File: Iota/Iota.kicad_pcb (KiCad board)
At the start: 2 copper layers, 31.8 x 54.6 mm, 25 parts, among them J1 USB_B_Mini, J2 Conn_01x12_Male, J3 Conn_01x12_Male, J4 ICSP, U1 ATmega32U4-AU, Y1 16MHz

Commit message: Working on PCB layout
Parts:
- moved J1 3.24 mm to (133.3, 61.8)
- moved C6 2.73 mm to (133.2, 66.1)
- moved R7 2.64 mm to (138.9, 66.8)
- moved R5 2.59 mm to (136.9, 66.8)
- moved D2 1.83 mm to (127.0, 62.1), turned to 270 degrees
- moved F1 1.52 mm to (133.4, 68.4)
- moved R11 1.40 mm to (127.0, 66.2), turned to 270 degrees
- moved C13 0.58 mm to (133.4, 70.9)
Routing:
- net UVCC: track 19.2 -> 0.09 mm
- net D+: track 17.3 -> 0.00 mm, vias 2 -> 0
- net VCC: track 14.2 -> 0.00 mm, vias 2 -> 0
- net Net-(D2-Pad2): track 3.77 -> 0.00 mm
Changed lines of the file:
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@@
     (thickness 1.6)
     (drawings 4)
-    (tracks 35)
+    (tracks 2)
     (zones 0)
     (modules 25)
@@
   )
   (module Resistors_SMD:R_0805 (layer F.Cu)
-    (at 140.0175 64.3865 90)
+    (at 138.938 66.7995 90)
     (descr "Resistor SMD 0805, reflow soldering, Vishay (see dcrcw.pdf)")
     (tags "resistor 0805")
@@
   )
   (module Connectors:USB_Micro-B (layer F.Cu)
-    (at 133.4135 58.6105 180)
+    (at 133.2865 61.849 180)
     (descr "Micro USB Type B Receptacle")
     (tags "USB USB_B USB_micro USB_OTG")
@@
   )
   (module Capacitors_SMD:C_0805 (layer F.Cu)
-    (at 133.366 70.2945)
+    (at 133.4295 70.866)
     (descr "Capacitor SMD 0805, reflow soldering, AVX (see smccp.pdf)")
     (tags "capacitor 0805")
@@
   )
   (module Resistors_SMD:R_0805 (layer F.Cu)
-    (at 137.8585 64.3865 90)
+    (at 136.906 66.7995 90)
     (descr "Resistor SMD 0805, reflow soldering, Vishay (see dcrcw.pdf)")
     (tags "resistor 0805")
@@
   )
   (module Resistors_SMD:R_0805 (layer F.Cu)
-    (at 127.8915 67.2465)
+    (at 127 66.167 270)
     (descr "Resistor SMD 0805, reflow soldering, Vishay (see dcrcw.pdf)")
     (tags "resistor 0805")
     (attr smd)
-    (fp_text reference R11 (at 0.061 0.0635) (layer F.SilkS)
-      (effects (font (size 1 1) (thickness 0.15)))
-    )
-    (fp_text value 1K (at -0.0025 0.127) (layer F.Fab)
-      (effects (font (size 1 1) (thickness 0.15)))
-    )
-    (fp_text user %R (at 0 0) (layer F.Fab)
+    (fp_text reference R11 (at 0.061 0.0635 270) (layer F.SilkS)
+      (effects (font (size 1 1) (thickness 0.15)))
+    )
+    (fp_text value 1K (at -0.0025 0.127 270) (layer F.Fab)
+      (effects (font (size 1 1) (thickness 0.15)))
+    )
+    (fp_text user %R (at 0 0 270) (layer F.Fab)
       (effects (font (size 0.5 0.5) (thickness 0.075)))
     )
@@
     (fp_line (start 1.55 0.9) (end 1.55 -0.9) (layer F.CrtYd) (width 0.05))
     (fp_line (start 1.55 0.9) (end -1.55 0.9) (layer F.CrtYd) (width 0.05))
-    (pad 1 smd rect (at -0.95 0) (size 0.7 1.3) (layers F.Cu F.Paste F.Mask)
+    (pad 1 smd rect (at -0.95 0 270) (size 0.7 1.3) (layers F.Cu F.Paste F.Mask)
       (net 41 "Net-(D2-Pad2)"))
-    (pad 2 smd rect (at 0.95 0) (size 0.7 1.3) (layers F.Cu F.Paste F.Mask)
+    (pad 2 smd rect (at 0.95 0 270) (size 0.7 1.3) (layers F.Cu F.Paste F.Mask)
       (net 6 VCC))
     (model ${KISYS3DMOD}/Resistors_SMD.3dshapes/R_0805.wrl
@@
   )
   (module Capacitors_SMD:C_0805 (layer F.Cu)
-    (at 133.3025 63.373)
+    (at 133.239 66.1035)
     (descr "Capacitor SMD 0805, reflow soldering, AVX (see smccp.pdf)")
     (tags "capacitor 0805")
     (attr smd)
-    (fp_text reference C6 (at 0 -1.5) (layer F.SilkS)
+    (fp_text reference C6 (at 0 0) (layer F.SilkS)
       (effects (font (size 1 1) (thickness 0.15)))
     )
@@
   )
   (module Diodes_SMD:D_1206 (layer F.Cu)
-    (at 127.86686 63.713672 180)
+    (at 127 62.103 270)
     (descr "Diode SMD 1206, reflow soldering http://datasheets.avx.com/schottky.pdf")
     (tags "Diode 1206")
     (attr smd)
-    (fp_text reference D2 (at -0.02214 0.023172 180) (layer F.SilkS)
-      (effects (font (size 1 1) (thickness 0.15)))
-    )
-    (fp_text value red (at -0.02214 0.150172 180) (layer F.Fab)
+    (fp_text reference D2 (at -0.02214 0.023172 270) (layer F.SilkS)
+      (effects (font (size 1 1) (thickness 0.15)))
+    )
+    (fp_text value red (at -0.02214 0.150172 270) (layer F.Fab)
       (effects (font (size 1 1) (thickness 0.15)))
     )
@@
     (fp_line (start 0.127 0) (end 0.381 0) (layer F.Fab) (width 0.1))
     (fp_line (start -0.254 -0.254) (end -0.254 0.254) (layer F.Fab) (width 0.1))
-    (fp_text user %R (at -0.02214 0.023172 180) (layer F.Fab)
-      (effects (font (size 1 1) (thickness 0.15)))
-    )
-    (pad 2 smd rect (at 1.5 0 180) (size 1 1.6) (layers F.Cu F.Paste F.Mask)
+    (fp_text user %R (at -0.02214 0.023172 270) (layer F.Fab)
+      (effects (font (size 1 1) (thickness 0.15)))
+    )
+    (pad 2 smd rect (at 1.5 0 270) (size 1 1.6) (layers F.Cu F.Paste F.Mask)
       (net 41 "Net-(D2-Pad2)"))
-    (pad 1 smd rect (at -1.5 0 180) (size 1 1.6) (layers F.Cu F.Paste F.Mask)
+    (pad 1 smd rect (at -1.5 0 270) (size 1 1.6) (layers F.Cu F.Paste F.Mask)
       (net 1 GND))
     (model ${KISYS3DMOD}/Diodes_SMD.3dshapes/D_1206.wrl
@@
   )
   (module Resistors_SMD:R_1206 (layer F.Cu)
-    (at 133.35 66.8655)
+    (at 133.3605 68.3895)
     (descr "Resistor SMD 1206, reflow soldering, Vishay (see dcrcw.pdf)")
     (tags "resistor 1206")
     (attr smd)
-    (fp_text reference F1 (at 0.0635 -3.429) (layer F.SilkS)
+    (fp_text reference F1 (at 0.0635 0) (layer F.SilkS)
       (effects (font (size 1 1) (thickness 0.15)))
     )
@@
   (gr_line (start 149.225 55.1815) (end 149.225 109.7915) (layer Edge.Cuts) (width 0.15))
   (gr_line (start 117.5385 55.1815) (end 149.225 55.1815) (layer Edge.Cuts) (width 0.15))
-  (segment (start 132.1135 59.9605) (end 130.9135 59.9605) (width 0.25) (layer F.Cu) (net 1))
-  (segment (start 134.3025 66.368) (end 134.8 66.8655) (width 0.25) (layer F.Cu) (net 4))
-  (segment (start 134.3025 63.373) (end 134.3025 66.368) (width 0.25) (layer F.Cu) (net 4))
-  (segment (start 134.366 63.3095) (end 134.3025 63.373) (width 0.25) (layer F.Cu) (net 4))
-  (segment (start 134.7135 62.962) (end 134.3025 63.373) (width 0.25) (layer F.Cu) (net 4))
-  (segment (start 134.7135 59.9605) (end 134.7135 62.962) (width 0.25) (layer F.Cu) (net 4))
-  (segment (start 132.541483 76.327) (end 132.437273 76.22279) (width 0.25) (layer F.Cu) (net 4))
-  (segment (start 132.651276 76.327) (end 132.541483 76.327) (width 0.25) (layer F.Cu) (net 4))
-  (segment (start 135.191001 68.356501) (end 135.191001 73.787275) (width 0.25) (layer F.Cu) (net 4))
-  (segment (start 132.437273 76.22279) (end 131.836233 75.62175) (width 0.25) (layer F.Cu) (net 4))
-  (segment (start 135.191001 73.787275) (end 132.651276 76.327) (width 0.25) (layer F.Cu) (net 4))
-  (segment (start 134.8 67.9655) (end 135.191001 68.356501) (width 0.25) (layer F.Cu) (net 4))
-  (segment (start 134.8 66.8655) (end 134.8 67.9655) (width 0.25) (layer F.Cu) (net 4))
-  (segment (start 131.519 67.2465) (end 131.9 66.8655) (width 0.25) (layer F.Cu) (net 6))
-  (segment (start 128.8415 67.2465) (end 131.519 67.2465) (width 0.25) (layer F.Cu) (net 6))
-  (segment (start 131.9 69.8285) (end 132.366 70.2945) (width 0.25) (layer F.Cu) (net 6))
-  (segment (start 131.9 66.8655) (end 131.9 69.8285) (width 0.25) (layer F.Cu) (net 6))
-  (via (at 133.096 71.882) (size 0.8) (drill 0.4) (layers F.Cu B.Cu) (net 6))
-  (segment (start 132.366 71.152) (end 133.096 71.882) (width 0.25) (layer F.Cu) (net 6))
-  (segment (start 132.366 70.2945) (end 132.366 71.152) (width 0.25) (layer F.Cu) (net 6))
-  (via (at 135.916001 73.533) (size 0.8) (drill 0.4) (layers F.Cu B.Cu) (net 6))
-  (segment (start 134.747 73.533) (end 135.916001 73.533) (width 0.25) (layer B.Cu) (net 6))
-  (segment (start 133.096 71.882) (end 134.747 73.533) (width 0.25) (layer B.Cu) (net 6))
-  (segment (start 135.916001 73.946145) (end 134.806082 75.056064) (width 0.25) (layer F.Cu) (net 6))
-  (segment (start 135.916001 73.533) (end 135.916001 73.946145) (width 0.25) (layer F.Cu) (net 6))
-  (via (at 137.8585 66.4845) (size 0.8) (drill 0.4) (layers F.Cu B.Cu) (net 36))
-  (segment (start 137.8585 65.3365) (end 137.8585 66.4845) (width 0.25) (layer F.Cu) (net 36))
-  (via (at 129.6035 75.5015) (size 0.8) (drill 0.4) (layers F.Cu B.Cu) (net 36))
-  (segment (start 129.6035 75.651758) (end 130.704862 76.75312) (width 0.25) (layer F.Cu) (net 36))
-  (segment (start 129.6035 75.5015) (end 129.6035 75.651758) (width 0.25) (layer F.Cu) (net 36))
-  (segment (start 134.493 66.4845) (end 129.6035 71.374) (width 0.25) (layer B.Cu) (net 36))
-  (segment (start 129.6035 71.374) (end 129.6035 75.5015) (width 0.25) (layer B.Cu) (net 36))
-  (segment (start 137.8585 66.4845) (end 134.493 66.4845) (width 0.25) (layer B.Cu) (net 36))
-  (segment (start 126.36686 66.67186) (end 126.9415 67.2465) (width 0.25) (layer F.Cu) (net 41))
-  (segment (start 126.36686 63.713672) (end 126.36686 66.67186) (width 0.25) (layer F.Cu) (net 41))
+  (segment (start 132.177 63.199) (end 130.977 63.199) (width 0.25) (layer F.Cu) (net 1))
+  (segment (start 134.5565 66.04) (end 134.493 66.1035) (width 0.25) (layer F.Cu) (net 4))
   (zone (net 1) (net_name GND) (layer F.Cu) (hatch edge 0.508)
     (connect_pads (clearance 0.508))

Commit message: Still faffing around laying out tracks
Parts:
- moved D1 30.6 mm to (125.5, 65.5), turned to 90 degrees
- moved R4 21.9 mm to (125.5, 69.7), turned to 270 degrees
- moved R6 18.0 mm to (126.0, 90.2), turned to 90 degrees
- moved D3 17.2 mm to (126.0, 94.1)
- moved R11 15.2 mm to (141.8, 69.6)
- moved D2 15.2 mm to (141.8, 65.5)
- moved C3 9.79 mm to (141.0, 77.0), turned to 0 degrees
- moved F1 5.99 mm to (139.2, 69.8), turned to 90 degrees
- moved R5 5.06 mm to (132.5, 69.2)
- moved R7 5.00 mm to (134.6, 69.2)
- moved C6 4.92 mm to (136.9, 69.4), turned to 90 degrees
- moved C14 3.18 mm to (136.3, 91.2), turned to 180 degrees
- moved J2 2.80 mm to (122.2, 99.3)
- moved J1 2.79 mm to (133.3, 64.6)
- moved C1 2.70 mm to (139.6, 75.1), turned to 180 degrees
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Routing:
- net GND: track 1.20 -> 0.00 mm
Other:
- board outline removed

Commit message: Still fiddling with PCB layout
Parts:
- moved C14 0.84 mm to (137.2, 91.1)
- moved U1 0.80 mm to (134.0, 82.6), turned to 225 degrees
- moved R2 0.76 mm to (125.8, 86.7)

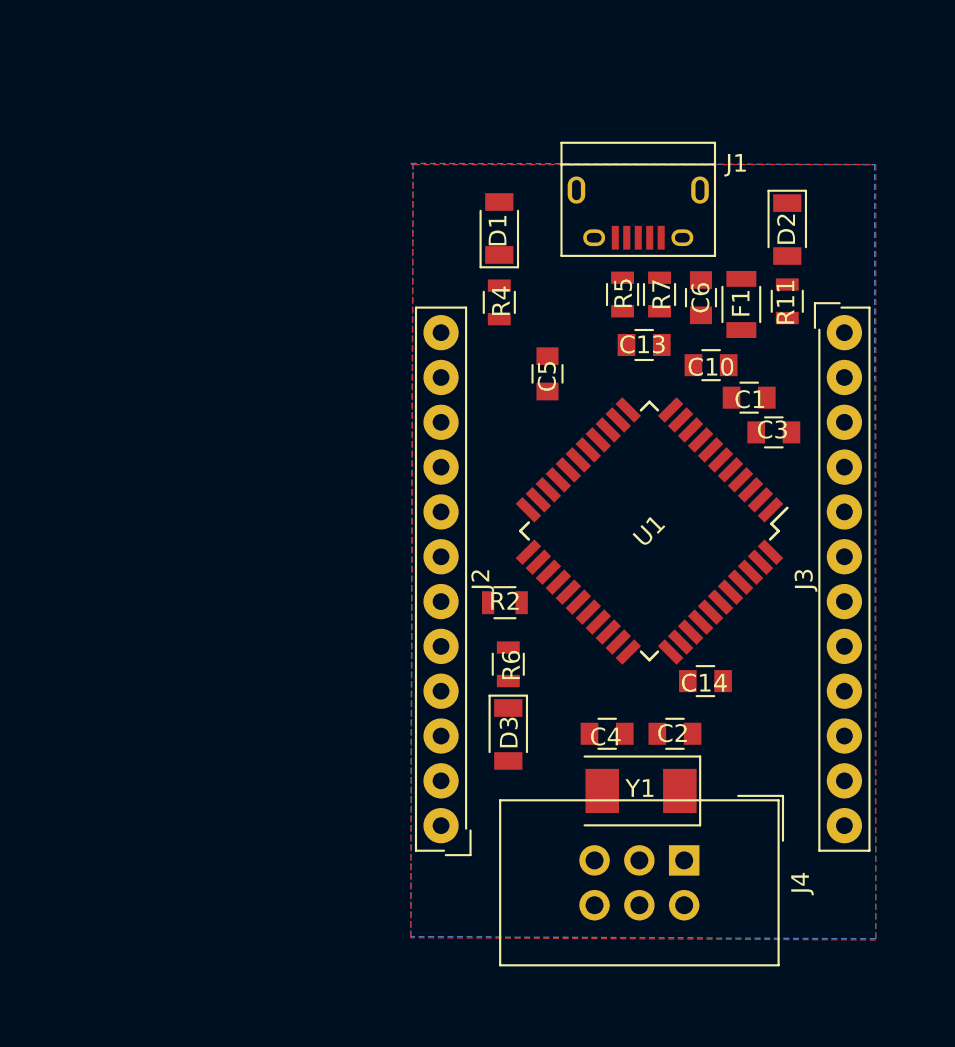
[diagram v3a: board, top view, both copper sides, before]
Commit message: Move to Teensy 2.0 clone
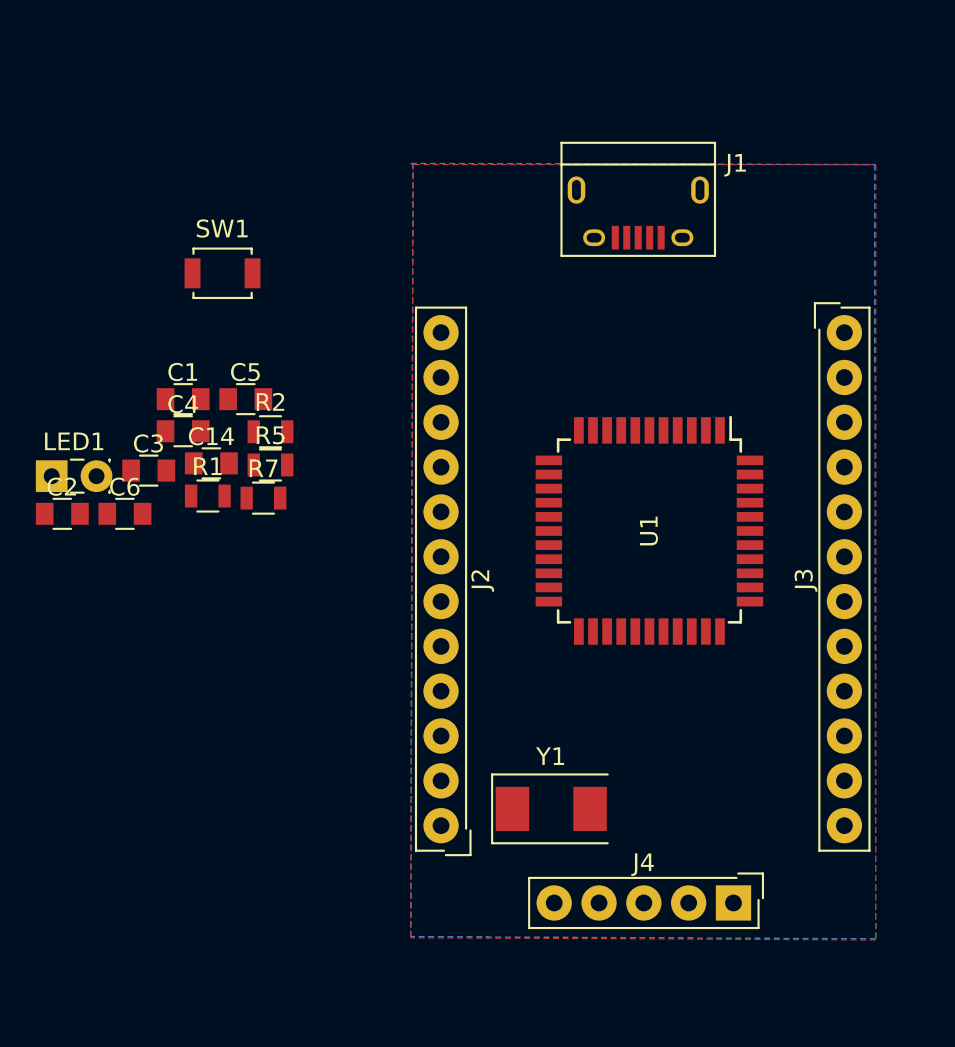
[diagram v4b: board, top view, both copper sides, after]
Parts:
- removed C10: 1uF, Capacitors_SMD:C_0805
- removed C13: 10uF, Capacitors_SMD:C_0805
- removed D1: yellow, Diodes_SMD:D_1206
- removed D2: red, Diodes_SMD:D_1206
- removed D3: green, Diodes_SMD:D_1206
- removed F1: 500mA, Resistors_SMD:R_1206
- removed R11: 1K, Resistors_SMD:R_0805
- removed R4, R6: 330, Resistors_SMD:R_0805
- added LED1: red, LEDs:LED_Rectangular_W3.9mm_H1.8mm, F.Cu at (100.1, 79.5)
- added R1: 1K0, Resistors_SMD:R_0805, F.Cu at (109.0, 80.6)
- added SW1: SW_DIP_x01, Buttons_Switches_SMD:SW_SPST_B3U-1000P, F.Cu at (109.8, 68.0)
- C2, C4: value 22pF -> 10pF
- J4: value ICSP -> Conn_01x05_Male; footprint Connectors_IDC:IDC-Header_2x03_Pitch2.54mm_Straight -> Connectors_Samtec:SL-105-X-XX_1x05
- R2: value 10K -> 1K0
- moved C2 36.9 mm to (100.7, 81.6)
- moved C3 35.5 mm to (105.6, 79.2)
- moved C6 34.9 mm to (104.3, 81.6), turned to 0 degrees
- moved C1 32.1 mm to (107.6, 75.1), turned to 0 degrees
- moved C14 30.6 mm to (109.2, 78.8), turned to 0 degrees
- moved C4 29.5 mm to (107.6, 77.0), turned to 0 degrees
- moved R7 25.2 mm to (112.1, 80.8), turned to 0 degrees
- moved R5 22.2 mm to (112.5, 78.9), turned to 0 degrees
- moved C5 17.2 mm to (111.1, 75.1), turned to 0 degrees
- moved R2 16.4 mm to (112.5, 77.0)
- moved Y1 5.19 mm to (128.4, 98.4), turned to 0 degrees
- moved J4 3.69 mm to (138.7, 103.7)
- turned U1 to 270 degrees
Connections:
- C14 pad 2: VCC -> Vcc
- C3 pad 2: VCC -> Vcc
- C6 pad 2: UVCC -> Vcc
- J1 pad 1: UVCC -> Vcc
- J2 pad 1: D9 -> C7
- J2 pad 10: GND -> B1
- J2 pad 11: RXI -> B0
- J2 pad 12: TXO -> GND
- J2 pad 2: D8 -> C6
- J2 pad 3: D7 -> D3
- J2 pad 4: D6 -> D2
- J2 pad 5: D5 -> D1
- J2 pad 6: D4 -> D0
- J2 pad 7: D3 -> B7
- J2 pad 8: D2 -> B3
- J2 pad 9: GND -> B2
- J3 pad 1: Net-(J3-Pad1) -> Vcc
- J3 pad 10: MISO -> B4
- J3 pad 11: MOSI -> D7
- J3 pad 12: D10 -> D6
- J3 pad 2: GND -> F0
- J3 pad 3: RESET -> F1
- J3 pad 4: VCC -> F4
- J3 pad 5: A3 -> F5
- J3 pad 6: A2 -> F6
- J3 pad 7: A1 -> F7
- J3 pad 8: A0 -> B6
- J3 pad 9: SCK -> B5
- J4 pad 1: MISO -> D4
- J4 pad 2: VCC -> RESET
- J4 pad 3: SCK -> GND
- J4 pad 4: MOSI -> Vcc
- J4 pad 5: RESET -> D5
- R2 pad 1: RESET -> Net-(LED1-Pad1)
- R2 pad 2: VCC -> GND
- U1 pad 1: D7 -> E6
- U1 pad 10: MOSI -> B2
- U1 pad 11: MISO -> B3
- U1 pad 12: D11 -> B7
- U1 pad 14: VCC -> Vcc
- U1 pad 18: D3 -> D0
- U1 pad 19: D2 -> D1
- U1 pad 2: UVCC -> Vcc
- U1 pad 20: RXI -> D2
- U1 pad 21: TXO -> D3
- U1 pad 22: Net-(R6-Pad2) -> D5
- U1 pad 24: VCC -> Vcc
- U1 pad 26: D12 -> D6
- U1 pad 27: D6 -> D7
- U1 pad 28: D8 -> B4
- U1 pad 29: D9 -> B5
- U1 pad 30: D10 -> B6
- U1 pad 31: D5 -> C6
- U1 pad 32: D13 -> C7
- U1 pad 33: GND -> Net-(R1-Pad2)
- U1 pad 34: VCC -> Vcc
- U1 pad 36: A0 -> F7
- U1 pad 37: A1 -> F6
- U1 pad 38: A2 -> F5
- U1 pad 39: A3 -> F4
- U1 pad 40: A4 -> F1
- U1 pad 41: A5 -> F0
- U1 pad 44: VCC -> Vcc
- U1 pad 7: UVCC -> Vcc
- U1 pad 8: Net-(R4-Pad2) -> B0
- U1 pad 9: SCK -> B1

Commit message: Switch over to Teensy 2 clone
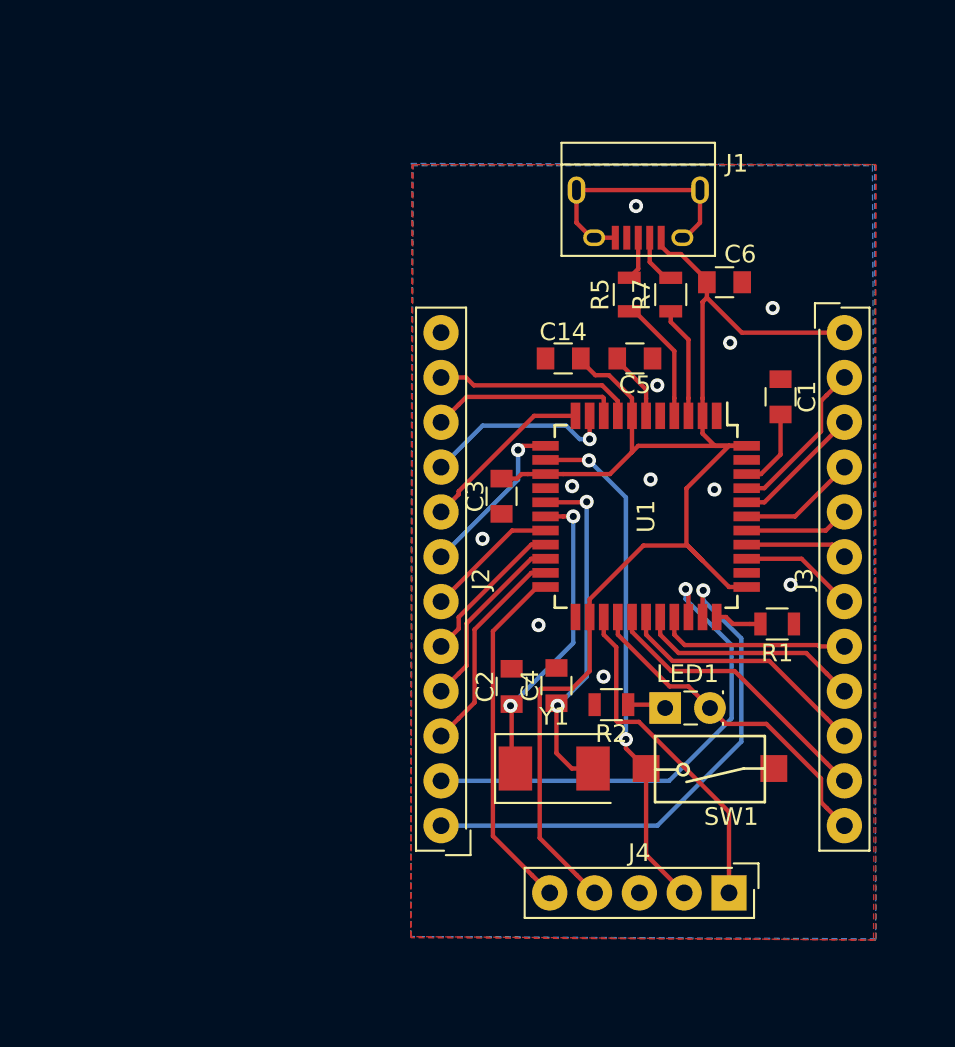
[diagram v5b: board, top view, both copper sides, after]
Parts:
- SW1: footprint Buttons_Switches_SMD:SW_SPST_B3U-1000P -> Iota:Switch
- moved SW1 39.4 mm to (137.4, 96.1), turned to 180 degrees
- moved LED1 37.2 mm to (134.9, 92.6)
- moved C6 36.4 mm to (138.2, 68.5), turned to 180 degrees
- moved C1 33.9 mm to (141.4, 75.0), turned to 270 degrees
- moved R1 33.1 mm to (141.2, 87.9), turned to 180 degrees
- moved C2 27.3 mm to (126.2, 91.4), turned to 90 degrees
- moved R7 25.8 mm to (135.2, 69.2), turned to 90 degrees
- moved C4 25.6 mm to (128.7, 91.4), turned to 90 degrees
- moved R2 24.7 mm to (131.8, 92.5), turned to 180 degrees
- moved R5 22.5 mm to (132.8, 69.2), turned to 90 degrees
- moved C5 22.2 mm to (133.2, 72.8), turned to 180 degrees
- moved C14 20.8 mm to (129.1, 72.8)
- moved C3 20.0 mm to (125.6, 80.6), turned to 90 degrees
- moved Y1 2.29 mm to (128.6, 96.1)
- moved U1 0.85 mm to (133.8, 81.8)
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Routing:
- net Vcc: track 0.00 -> 84.8 mm
- net C7: track 0.00 -> 30.0 mm, vias 0 -> 1
- net RESET: track 0.00 -> 29.6 mm, vias 0 -> 2
- net C6: track 0.00 -> 28.0 mm, vias 0 -> 1
- net D5: track 0.00 -> 20.7 mm
- net Net-(C4-Pad1): track 0.00 -> 19.8 mm, vias 0 -> 2
- net D4: track 0.00 -> 19.3 mm
- net D6: track 0.00 -> 19.1 mm
- net Net-(C2-Pad1): track 0.00 -> 17.5 mm, vias 0 -> 2
- net D7: track 0.00 -> 16.4 mm
- net B4: track 0.00 -> 14.6 mm
- net GND: track 0.00 -> 14.6 mm, vias 0 -> 11
- net B5: track 0.00 -> 12.8 mm
- net D3: track 0.00 -> 12.2 mm
- net B0: track 0.00 -> 11.4 mm
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
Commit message: Finalizing PCB layout
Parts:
- moved C6 3.95 mm to (141.0, 65.7)
- moved C5 3.64 mm to (130.0, 71.1), turned to 270 degrees
- moved C14 2.22 mm to (127.7, 71.1), turned to 270 degrees
- moved LED1 1.15 mm to (136.0, 92.5)
- moved R2 1.14 mm to (133.0, 92.4)
- moved Y1 0.11 mm to (128.7, 96.1)
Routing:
- net GND: track 14.6 -> 26.1 mm, vias 11 -> 15
- net Vcc: track 84.8 -> 92.8 mm
- net C6: track 28.0 -> 22.6 mm
- net Net-(C5-Pad2): track 3.93 -> 6.16 mm
- net D6: track 19.1 -> 20.9 mm
- net D4: track 19.3 -> 18.6 mm
